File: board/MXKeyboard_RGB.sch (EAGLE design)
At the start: 363 parts, among them Q1 DMN65D8L, Q2 DMP2240UDM, U1 TLC5947RHBT, U10 TLC5947RHBT, U11 ATXMEGA256A3U-MH, U12 NTS0104, U14 TC1015-3.3VCT713, U15 74HC238BQ, U16 74HC238BQ, U17 74HC238BQ, U18 TLC5947RHBT, U19 TLC5947RHBT, U2 TLC5947RHBT, U20 TLC5947RHBT, U21 TLC5947RHBT, U22 TLC5947RHBT, U3 TLC5947RHBT, U4 TLC5947RHBT, U5 TLC5947RHBT, U6 TLC5947RHBT, U7 TLC5947RHBT, U8 TLC5947RHBT, U9 TLC5947RHBT

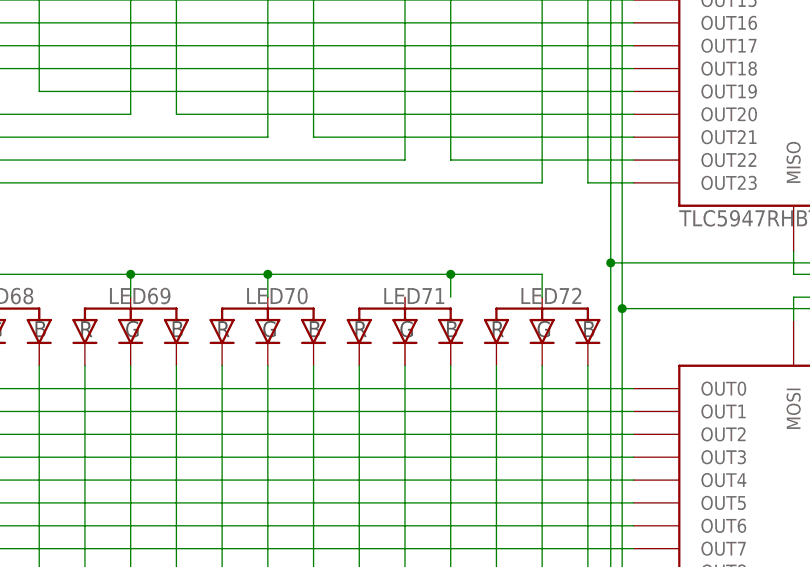
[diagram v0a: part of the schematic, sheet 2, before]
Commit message: Added some fixes for hardware borkage we've discovered
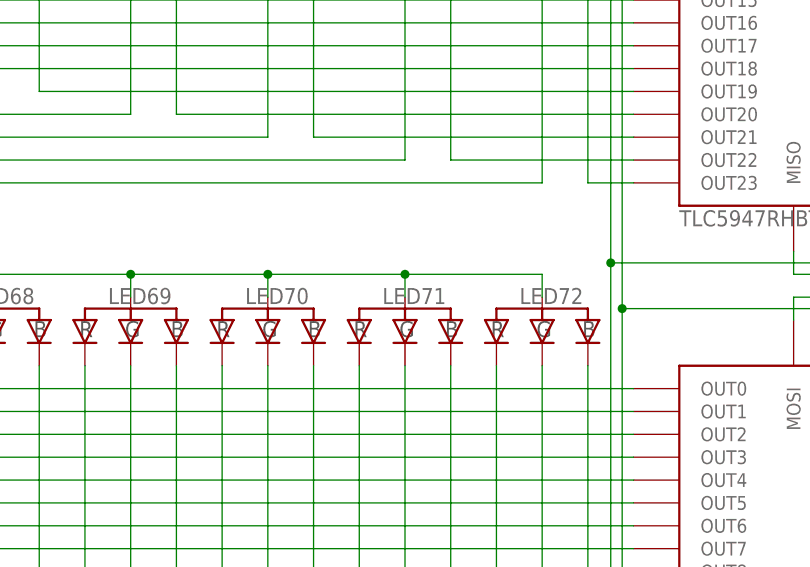
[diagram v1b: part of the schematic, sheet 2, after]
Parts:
- OSC1: ALT_MFR (none) -> Multicomp; ALT_MPN (none) -> MCSJK-3N-16.00-3.3-25-B; ALT_OC_FARNELL (none) -> 2854286; ALT_URL (none) -> https://uk.farnell.com/multicomp/mcsjk-3n-16-00-3-3-25-b/os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
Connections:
- net +5V: now also LED71.A
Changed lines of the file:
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@@
 <part name="SUPPLY22" library="supply2" deviceset="GND" device=""/>
 <part name="OSC1" library="MXKeyboard" deviceset="CXO" device="-7M" value="16MHz">
+<attribute name="ALT_MFR" value="Multicomp"/>
+<attribute name="ALT_MPN" value="MCSJK-3N-16.00-3.3-25-B"/>
+<attribute name="ALT_OC_FARNELL" value="2854286"/>
+<attribute name="ALT_URL" value="https://uk.farnell.com/multicomp/mcsjk-3n-16-00-3-3-25-b/oscillator-16mhz-3-2mm-x-2-5mm/dp/2854286"/>
 <attribute name="MFR" value="IQD"/>
 <attribute name="MPN" value="LFSPXO025494"/>
@@
 <wire x1="353.06" y1="259.08" x2="342.9" y2="259.08" width="0.1524" layer="91"/>
 <wire x1="414.02" y1="256.54" x2="414.02" y2="259.08" width="0.1524" layer="91"/>
-<wire x1="403.86" y1="259.08" x2="414.02" y2="259.08" width="0.1524" layer="91"/>
-<wire x1="403.86" y1="256.54" x2="403.86" y2="259.08" width="0.1524" layer="91"/>
-<junction x="403.86" y="259.08"/>
-<wire x1="403.86" y1="259.08" x2="383.54" y2="259.08" width="0.1524" layer="91"/>
+<wire x1="398.78" y1="259.08" x2="414.02" y2="259.08" width="0.1524" layer="91"/>
+<wire x1="398.78" y1="256.54" x2="398.78" y2="259.08" width="0.1524" layer="91"/>
+<junction x="398.78" y="259.08"/>
+<wire x1="398.78" y1="259.08" x2="383.54" y2="259.08" width="0.1524" layer="91"/>
 <wire x1="383.54" y1="259.08" x2="383.54" y2="256.54" width="0.1524" layer="91"/>
 <junction x="383.54" y="259.08"/>
@@
 <pinref part="LED62" gate="G$1" pin="A"/>
 <pinref part="LED68" gate="G$1" pin="A"/>
+<pinref part="LED71" gate="G$1" pin="A"/>
 </segment>
 <segment>
@@
 <attribute name="OC_FARNELL" x="228.6" y="205.74" size="1.27" layer="96" display="off"/>
 <attribute name="URL" x="228.6" y="205.74" size="1.27" layer="96" display="off"/>
+<attribute name="ALT_OC_FARNELL" x="228.6" y="205.74" size="1.778" layer="96" display="off"/>
+<attribute name="ALT_URL" x="228.6" y="205.74" size="1.778" layer="96" display="off"/>
+<attribute name="ALT_MFR" x="228.6" y="205.74" size="1.778" layer="96" display="off"/>
+<attribute name="ALT_MPN" x="228.6" y="205.74" size="1.778" layer="96" display="off"/>
 </instance>
 <instance part="+3V14" gate="G$1" x="228.6" y="228.6" smashed="yes">
